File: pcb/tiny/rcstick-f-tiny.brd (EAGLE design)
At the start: 15.4 x 32 mm, 41 parts, among them J1 MOLEX_48037-0001, J2 2212S, SW1 SKRPACE010, U1 STM32F042K6U6, U2 CC2500, U3 MCP1703AT-3302E/CB, X1 16MHz/10pF, X2 26MHz/9pF, X3 (50 Ohm)

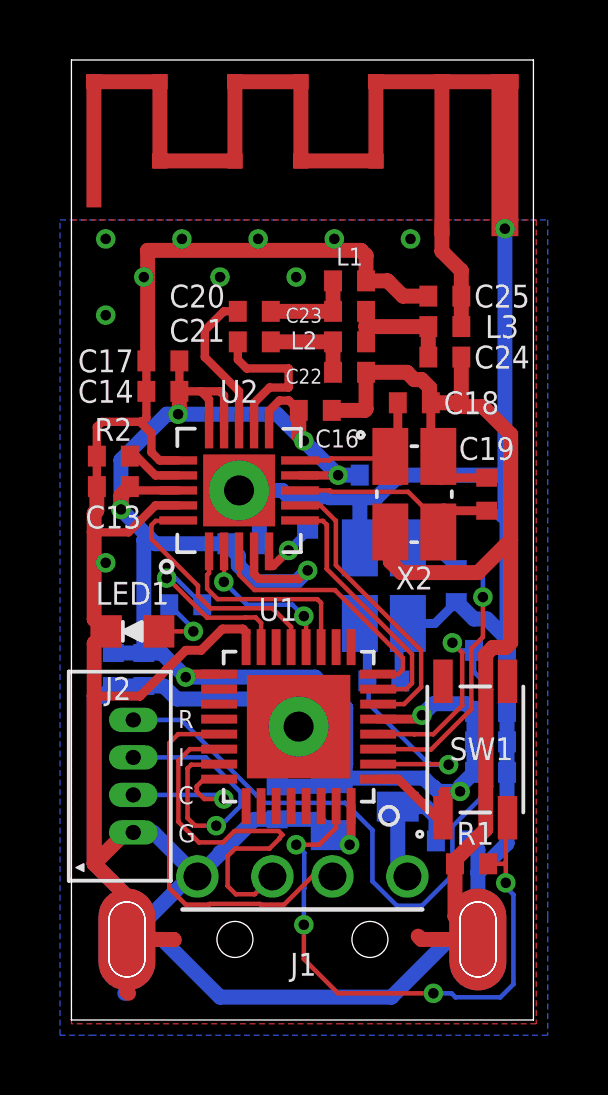
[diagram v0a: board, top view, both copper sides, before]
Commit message: change RF analog artwork for tiny version
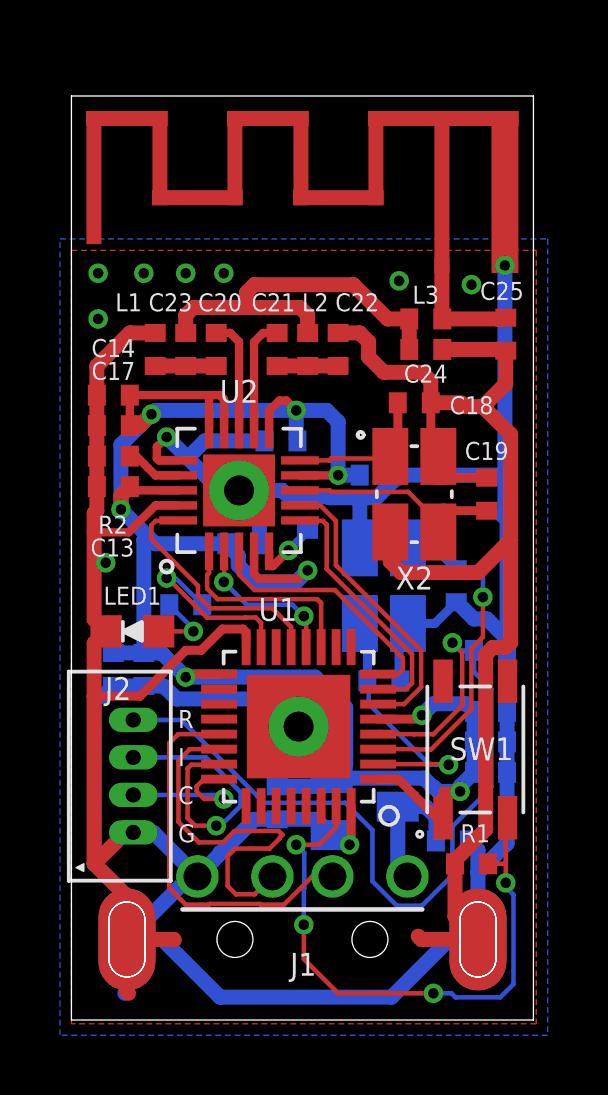
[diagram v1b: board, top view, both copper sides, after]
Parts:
- moved L1 6.87 mm to (2.79, 22.4), turned to 270 degrees
- moved C23 5.61 mm to (3.81, 22.4), turned to 90 degrees
- moved C17 2.72 mm to (1.40, 19.8)
- moved C25 2.40 mm to (14.5, 22.9), turned to 270 degrees
- moved C20 1.80 mm to (4.83, 22.4), turned to 270 degrees
- moved C14 1.66 mm to (1.40, 20.8)
- moved C16 1.53 mm to (6.99, 19.3), flipped to the bottom
- moved L2 1.42 mm to (7.87, 22.4), turned to 270 degrees
- moved X3 1.23 mm to (0.00, 30.6)
- moved C22 0.85 mm to (8.89, 22.4), turned to 90 degrees
- moved C21 0.80 mm to (6.86, 22.4), turned to 270 degrees
- moved C24 0.68 mm to (11.8, 22.4)
- moved L3 0.68 mm to (11.8, 23.4)
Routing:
- net N$10: track 4.11 -> 13.0 mm
- net GND: track 183.9 -> 177.5 mm, vias 11 -> 10
- net +3V3: track 67.3 -> 70.0 mm
- net RF_P: track 5.29 -> 3.81 mm
- net RF_N: track 5.14 -> 3.81 mm
- net N$5: track 3.09 -> 2.03 mm
- net N$9: track 3.09 -> 2.03 mm
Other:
- board size 15.4 x 32 mm -> 15.4 x 30.8 mm

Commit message: fix minor issue of tiny artwork
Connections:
- net GND: no longer U1.16, U1.32
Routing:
- net GND: track 177.5 -> 168.9 mm, vias 10 -> 9
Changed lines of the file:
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@@
 <text x="13.081" y="22.733" size="1.8" layer="22" rot="MR0">rcstick</text>
 <text x="5.334" y="22.733" size="1.2" layer="22" rot="MR0">V1.1</text>
-<rectangle x1="5.4" y1="11.811" x2="5.588" y2="12.88" layer="41"/>
 <rectangle x1="9.49" y1="6.731" x2="9.725" y2="7.6" layer="41"/>
 <rectangle x1="2.999" y1="18.8" x2="4.2" y2="19.04" layer="41"/>
@@
 <contactref element="C5" pad="2"/>
 <contactref element="C4" pad="2"/>
-<contactref element="U1" pad="16"/>
-<contactref element="U1" pad="32"/>
 <contactref element="C8" pad="2"/>
 <contactref element="C9" pad="2"/>
@@
 <wire x1="12.319" y1="18.076" x2="12.23" y2="18.165" width="0.5" layer="1"/>
 <wire x1="12.23" y1="18.165" x2="12.23" y2="18.786" width="0.5" layer="1"/>
-<contactref element="U1" pad="VSS"/>
-<contactref element="U1" pad="VSSH"/>
-<via x="9.271" y="5.842" extent="1-16" drill="0.35"/>
-<wire x1="8.702" y1="6.162" x2="8.679" y2="6.162" width="0.5" layer="16"/>
 <wire x1="13.55" y1="2.685" x2="12.785" y2="3.45" width="0.5" layer="1"/>
 <wire x1="12.785" y1="3.45" x2="12.785" y2="5.207" width="0.5" layer="1"/>
@@
 <wire x1="0.762" y1="5.207" x2="0.758" y2="5.211" width="0.5" layer="1"/>
 <wire x1="0.758" y1="5.211" x2="0.758" y2="10.795" width="0.5" layer="1"/>
-<wire x1="2.286" y1="10.795" x2="0.758" y2="10.795" width="0.3" layer="1"/>
-<wire x1="3.1802" y1="11.6892" x2="2.286" y2="10.795" width="0.3" layer="1"/>
-<wire x1="3.1802" y1="11.690875" x2="3.1802" y2="11.6892" width="0.3" layer="1"/>
 <wire x1="0.758" y1="12.555" x2="1.157" y2="12.954" width="0.5" layer="1"/>
 <wire x1="0.758" y1="10.795" x2="0.758" y2="12.555" width="0.5" layer="1"/>
@@
 <wire x1="13.55" y1="2.685" x2="11.666" y2="2.685" width="0.5" layer="1"/>
 <wire x1="11.666" y1="2.685" x2="11.557" y2="2.794" width="0.5" layer="1"/>
-<wire x1="8.679" y1="6.162" x2="8.951" y2="6.162" width="0.5" layer="16"/>
-<wire x1="9.271" y1="5.842" x2="8.951" y2="6.162" width="0.5" layer="16"/>
-<wire x1="9.271" y1="5.842" x2="9.323" y2="5.894" width="0.3" layer="1"/>
-<wire x1="9.323" y1="7.129" x2="9.323" y2="5.894" width="0.3" layer="1"/>
 <wire x1="6.265" y1="15.875" x2="6.265" y2="16.722" width="0.5" layer="16"/>
 <wire x1="5.588" y1="17.399" x2="5.588" y2="17.653" width="0.5" layer="16"/>
 <wire x1="6.265" y1="16.722" x2="5.588" y2="17.399" width="0.5" layer="16"/>
 <wire x1="11.98" y1="20.574" x2="11.938" y2="20.616" width="0.5" layer="1"/>
-<wire x1="4.324875" y1="12.3242" x2="3.813525" y2="12.3242" width="0.3" layer="1"/>
-<wire x1="3.813525" y1="12.3242" x2="3.1802" y2="11.690875" width="0.3" layer="1"/>
-<wire x1="5.823" y1="12.9246" x2="5.715" y2="13.0326" width="0.3" layer="1"/>
-<wire x1="5.715" y1="13.0326" x2="5.033275" y2="13.0326" width="0.3" layer="1"/>
-<wire x1="5.033275" y1="13.0326" x2="4.324875" y2="12.3242" width="0.3" layer="1"/>
 <contactref element="C6" pad="2"/>
 <contactref element="C7" pad="2"/>
@@
 <wire x1="2.413" y1="11.134" x2="3.07390625" y2="11.134" width="0.5" layer="16"/>
 <wire x1="3.07390625" y1="11.134" x2="3.50770625" y2="10.7002" width="0.5" layer="16"/>
-<wire x1="6.6518" y1="10.7002" x2="7.573" y2="9.779" width="0.5" layer="16"/>
-<wire x1="3.50770625" y1="10.7002" x2="6.6518" y2="10.7002" width="0.5" layer="16"/>
+<wire x1="6.6518" y1="10.7002" x2="3.50770625" y2="10.7002" width="0.5" layer="16"/>
 <wire x1="0.847" y1="17.78" x2="0.847" y2="18.796" width="0.5" layer="1"/>
 <wire x1="0.847" y1="18.796" x2="0.847" y2="19.812" width="0.5" layer="1"/>
@@
 <wire x1="14.478" y1="21.209" x2="13.716" y2="20.447" width="0.5" layer="1"/>
 <wire x1="14.478" y1="22.31" x2="14.478" y2="21.209" width="0.5" layer="1"/>
-<wire x1="5.823" y1="12.429" x2="5.823" y2="12.9246" width="0.28" layer="1"/>
 <wire x1="4.445" y1="19.304" x2="3.8735" y2="18.7325" width="0.5" layer="16"/>
 <wire x1="6.435" y1="19.304" x2="4.445" y2="19.304" width="0.5" layer="16"/>
@@
 <via x="0.889" y="24.892" extent="1-16" drill="0.35"/>
 <via x="0.889" y="23.368" extent="1-16" drill="0.35"/>
+<contactref element="U1" pad="VSS"/>
+<contactref element="U1" pad="VSSH"/>
+<wire x1="7.573" y1="9.779" x2="6.6518" y2="10.7002" width="0.5" layer="16"/>
 </signal>
 <signal name="+3V3" class="2">

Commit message: added QFN28 MCU version
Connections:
- net BOOT0: now also U1.32
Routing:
- net BOOT0: track 20.2 -> 22.4 mm
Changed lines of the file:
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@@
 <wire x1="7.747" y1="2.032" x2="8.89" y2="0.889" width="0.1524" layer="1"/>
 <wire x1="8.89" y1="0.889" x2="12.065" y2="0.889" width="0.1524" layer="1"/>
+<contactref element="U1" pad="32"/>
+<wire x1="9.323" y1="7.129" x2="9.323" y2="6.148" width="0.1524" layer="1"/>
+<wire x1="9.017" y1="5.842" x2="8.255" y2="5.842" width="0.1524" layer="1"/>
+<wire x1="9.323" y1="6.148" x2="9.017" y2="5.842" width="0.1524" layer="1"/>
 </signal>
 <signal name="NRST">
